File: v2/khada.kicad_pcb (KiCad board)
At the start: 2 copper layers, 154.2 x 111.4 mm, 60 parts, among them J1 MJ-4PP-9, SW1 SW_Push, SW10 SW_Push, SW11 SW_Push, SW12 SW_Push, SW13 SW_Push, SW14 SW_Push, SW15 SW_Push, SW16 SW_Push, SW17 SW_Push, SW18 SW_Push, SW19 SW_Push, SW2 SW_Push, SW20 SW_Push, SW21 SW_Push, SW22 SW_Push, SW23 RotaryEncoder_Switch, SW3 SW_Push, SW4 SW_Push, SW5 SW_Push, SW6 SW_Push, SW7 SW_Push, SW8 SW_Push, SW9 SW_Push, U1 YAAJ_WeAct_BlackPill_Part_Lik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

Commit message: save before moving mcu out
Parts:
- removed H4: Hole, used_footprints:M2_HOLE_PCB
- R1: footprint Resistor_THT:R_Axial_DIN0204_L3.6mm_D1.6mm_P5.08mm_Horizontal -> Resistor_THT:R_Axial_DIN0204_L3.6mm_D1.6mm_P7.62mm_Horizontal
- moved J1 63.3 mm to (207.5, 49.7), turned to 0 degrees
- moved R1 40.7 mm to (206.6, 66.3), turned to -90 degrees
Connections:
- J1 pad A: unconnected-(J1-PadA) -> DATA
- J1 pad B: DATA -> unconnected-(J1-PadB)
- J1 pad C: +5V -> GND
- J1 pad D: GND -> +5V
- R1 pad 1: +5V -> DATA
- R1 pad 2: DATA -> +5V
- U1 pad 18: +5V -> unconnected-(U1-5V)
- U1 pad 40: unconnected-(U1-Pad40) -> +5V
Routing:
- net GND: track 101.8 -> 0.00 mm, vias 2 -> 0
- net DATA: track 36.8 -> 29.5 mm
- net +5V: track 28.4 -> 31.9 mm
- net unconnected-(J1-PadA): track 2.45 -> 0.00 mm
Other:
- board size 154.2 x 111.4 mm -> 160.8 x 114.2 mm

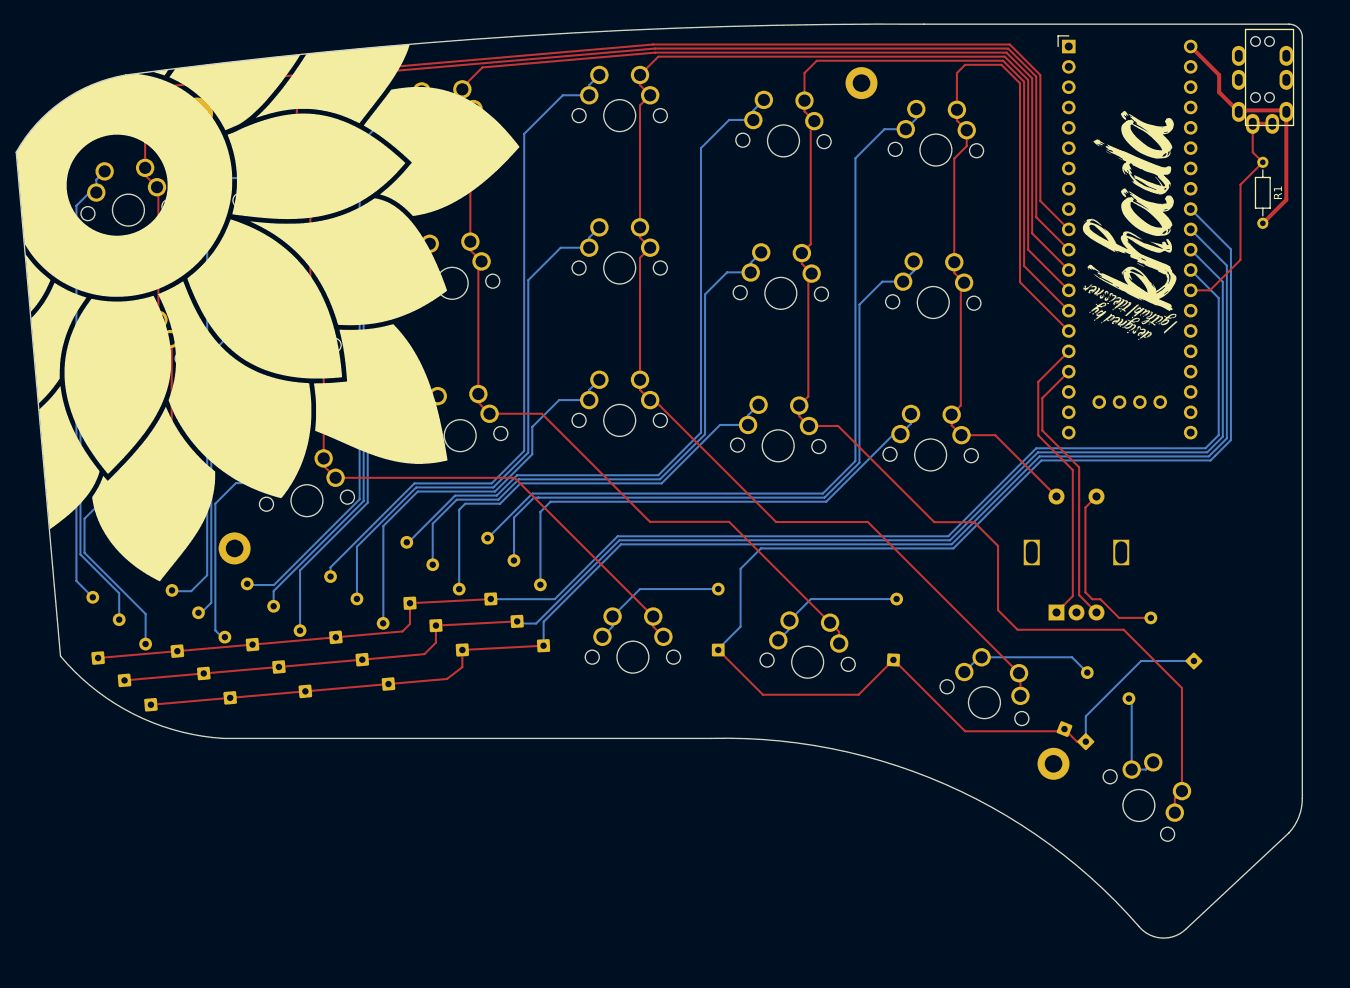
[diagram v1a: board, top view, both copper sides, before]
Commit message: add new switch for macros
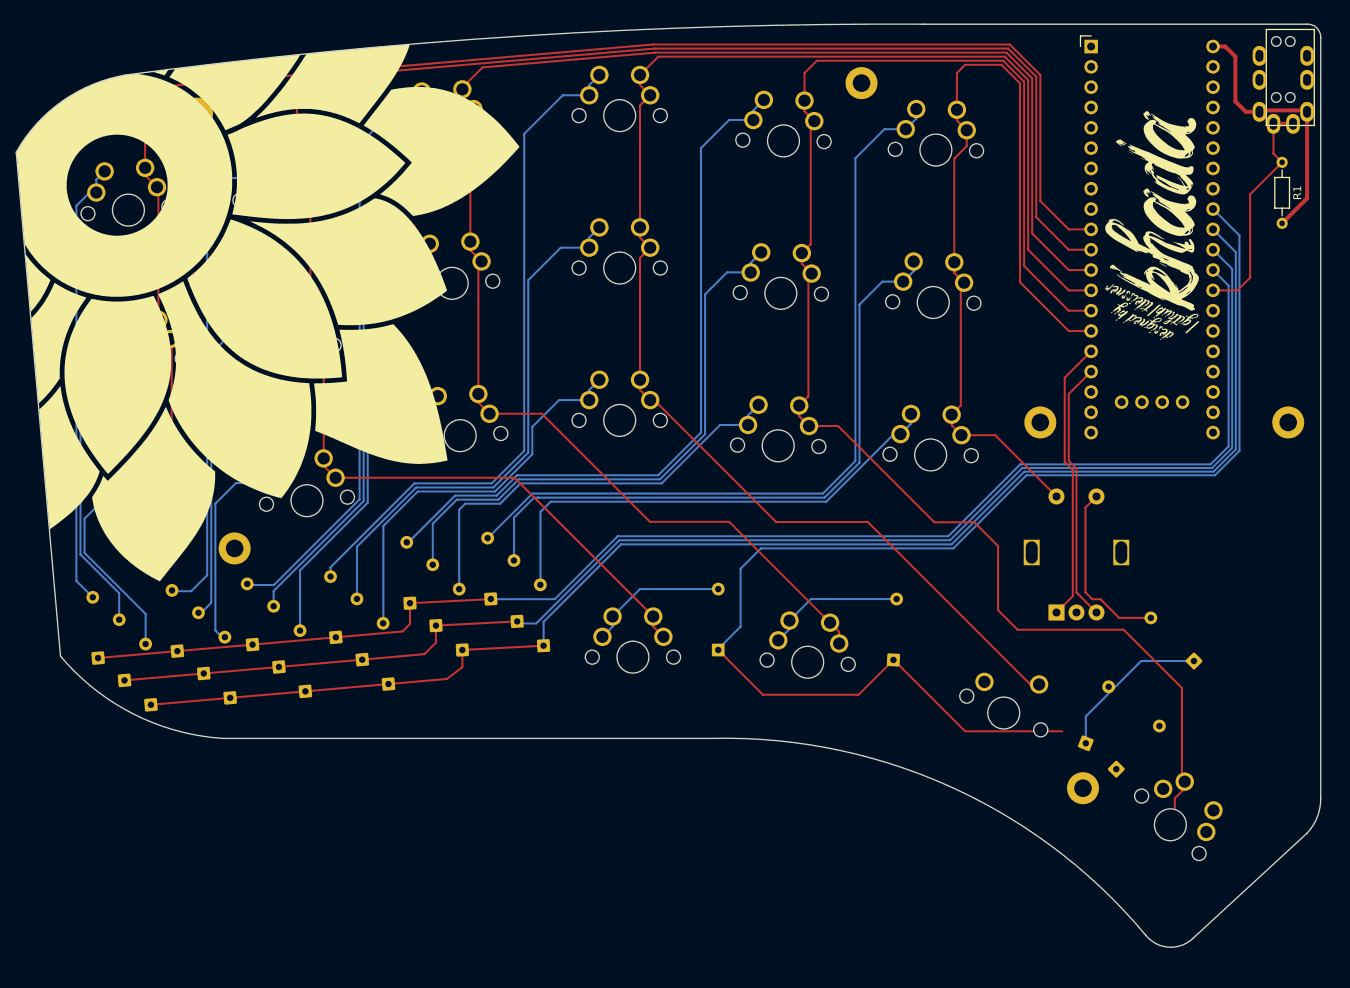
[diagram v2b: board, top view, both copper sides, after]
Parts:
- added H5: Hole, used_footprints:M2_HOLE_PCB, F.Cu at (209.8, 98.8)
- added H5: Hole, used_footprints:M2_HOLE_PCB, F.Cu at (178.8, 98.8)
- SW15: footprint marbastlib-mx:SW_MX_Reversible_1u_PadsOnBothLayers -> marbastlib-mx:SW_MX_1.25u
- moved D19 5.13 mm to (191.0, 139.4)
- moved H5 4.78 mm to (184.2, 144.5)
- moved SW19 4.62 mm to (195.1, 149.1)
- moved D15 3.21 mm to (185.9, 135.4)
- moved G*** 2.80 mm to (192.8, 72.4) (x2)
- moved U1 2.79 mm to (185.2, 51.8)
- moved SW15 2.74 mm to (174.2, 135.1), turned to -24.5 degrees
- moved G*** 2.73 mm to (193.1, 85.2)
- moved G*** 2.73 mm to (192.3, 85.2)
- moved J1 2.59 mm to (210.1, 49.7)
- moved R1 2.41 mm to (209.0, 66.3)
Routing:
- net Net-(D15-A): track 16.9 -> 0.00 mm
- net Net-(D19-A): track 12.9 -> 0.00 mm
- net col3: track 185.5 -> 188.5 mm
- net col5: track 106.7 -> 109.5 mm
- net col4: track 187.9 -> 190.7 mm
- net col2: track 198.8 -> 201.6 mm
- net col1: track 218.1 -> 220.9 mm
- net col0: track 186.1 -> 188.9 mm
- net row3: track 184.3 -> 181.7 mm
- net +5V: track 31.9 -> 33.8 mm
- net ROTB: track 34.3 -> 32.7 mm
- net ROTA: track 36.9 -> 35.3 mm
- net row0: track 173.8 -> 175.2 mm
- net row1: track 174.9 -> 176.2 mm
- net row2: track 178.0 -> 179.3 mm
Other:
- board size 160.8 x 114.2 mm -> 163.1 x 115.4 mm

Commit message: new sw placement, new macro sw, trrs jack now on top
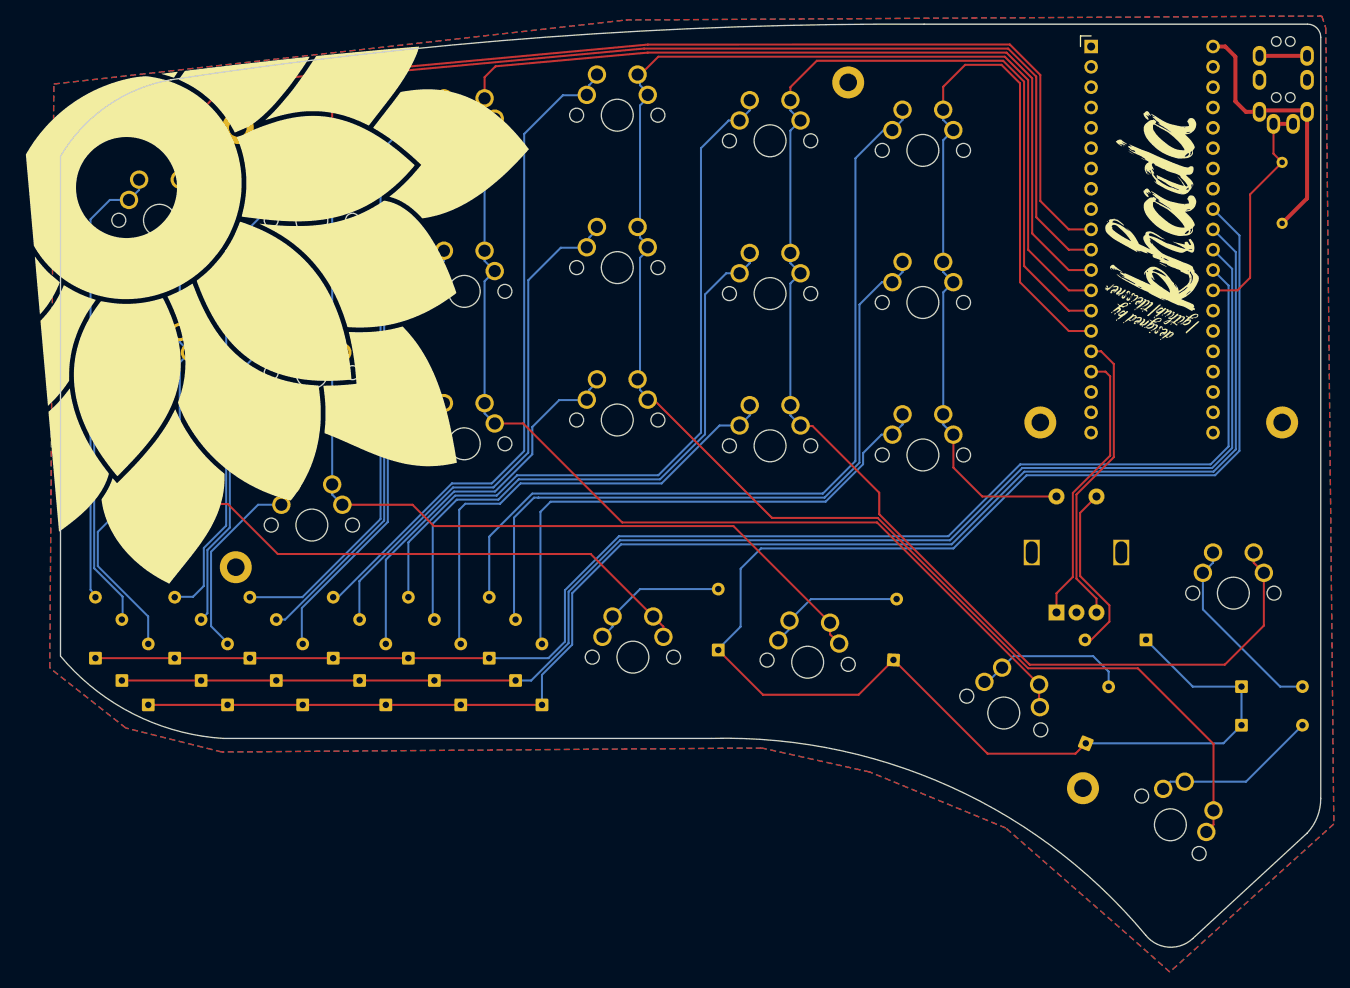
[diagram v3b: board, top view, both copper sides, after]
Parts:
- removed the G*** at (192.8, 72.4) (x2)
- removed the H5 at (209.8, 98.8)
- added D20: D_Small, acheron_Components:D_THT_7.62mm_copy, F.Cu at (207.8, 131.8)
- added G***: LOGO, logo:khada, F.Cu at (192.8, 72.4)
- added G***: LOGO, logo:khada, B.Cu at (192.8, 72.4)
- added H6: Hole, used_footprints:M2_HOLE_PCB, F.Cu at (209.0, 98.8)
- added SW20: SW_Push, marbastlib-mx:SW_MX_Reversible_1u_PadsOnBothLayers, F.Cu at (202.9, 120.1)
- SW12: renamed from SW15; footprint marbastlib-mx:SW_MX_1.25u -> marbastlib-mx:SW_MX_Reversible_1u_PadsOnBothLayers
- U1: footprint blackpills:YAAJ_WeAct_BlackPill_SWD_2 -> blackpills:YAAJ_WeAct_BlackPill_2_noSilk
- moved D16 17.0 mm to (207.8, 136.7), turned to 0 degrees
- moved D23 7.39 mm to (116.5, 130.3), turned to 90 degrees
- moved D21 7.39 mm to (109.9, 124.5), turned to 90 degrees
- moved D22 7.38 mm to (113.2, 127.3), turned to 90 degrees
- moved D24 7.11 mm to (188.2, 126.0), turned to 180 degrees
- moved D17 6.86 mm to (99.8, 124.5), turned to 90 degrees
- moved D18 6.86 mm to (103.1, 127.3), turned to 90 degrees
- moved D19 6.86 mm to (106.4, 130.3), turned to 90 degrees
- moved H1 5.40 mm to (78.5, 62.0)
- moved SW5 4.90 mm to (87.8, 73.5), turned to 0 degrees
- moved SW1 4.08 mm to (68.7, 73.5), turned to 0 degrees
- moved SW6 3.75 mm to (87.8, 92.6), turned to 0 degrees
- moved SW7 3.11 mm to (87.8, 111.6), turned to 0 degrees
- moved SW9 2.70 mm to (106.8, 63.4), turned to 0 degrees
- moved D14 2.59 mm to (93.7, 127.3), turned to 90 degrees
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- renumbered D9 to D10, D10 to D11, D15 to D12, D12 to D13, D13 to D14, D14 to D15, D19 to D16, D16 to D17, D17 to D18, D18 to D19, D20 to D21, D21 to D22, D22 to D23, D23 to D24, D7 to D4, D4 to D5, D5 to D6, D6 to D7, D11 to D8, D8 to D9, H5 to H4, SW9 to SW10, SW10 to SW11, SW12 to SW13, SW13 to SW14, SW14 to SW15, SW19 to SW16, SW16 to SW17, SW17 to SW18, SW18 to SW19, SW20 to SW21, SW21 to SW22, SW22 to SW23, SW23 to SW24, SW7 to SW4, SW4 to SW5, SW5 to SW6, SW6 to SW7, SW11 to SW8, SW8 to SW9
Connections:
- SW12 pad 2: col3 -> col2
- SW16 pad 2: col4 -> col3
- SW4 pad 2: col1 -> col0
- SW8 pad 2: col2 -> col1
- U1 pad 16: ROTA -> ROTB
- U1 pad 17: ROTB -> ROTA
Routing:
- net col0: track 188.9 -> 251.6 mm
- net col3: track 188.5 -> 224.2 mm
- net col2: track 201.6 -> 229.4 mm
- net row3: track 181.7 -> 206.4 mm
- net Net-(D20-A): track 0.00 -> 24.1 mm
- net Net-(D16-A): track 0.00 -> 20.7 mm
- net col1: track 220.9 -> 240.9 mm
- net Net-(D12-A): track 0.00 -> 19.6 mm
- net Net-(D23-A): track 61.5 -> 68.5 mm
- net unconnected-(J1-PadB): track 0.00 -> 5.95 mm
- net Net-(D22-A): track 81.1 -> 87.0 mm
- net Net-(D19-A): track 53.7 -> 59.3 mm
- net Net-(D21-A): track 98.7 -> 104.2 mm
- net Net-(D18-A): track 71.4 -> 76.7 mm
- net Net-(D17-A): track 88.9 -> 94.0 mm
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- added copper zone on B.Cu, net GND
- added copper zone on F.Cu, net GND
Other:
- board size 163.1 x 115.4 mm -> 157.5 x 115.4 mm
